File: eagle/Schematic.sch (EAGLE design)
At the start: 28 parts, among them U1 ATMEGA328P, X1 12MHz, X2 16MHz

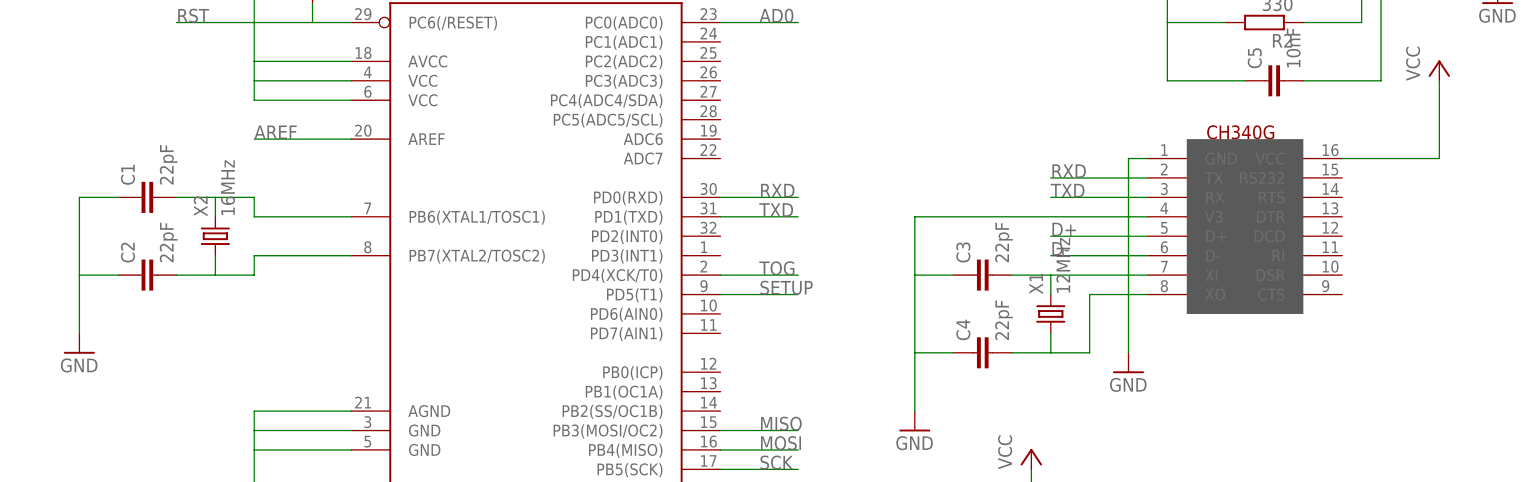
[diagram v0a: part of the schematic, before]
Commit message: Added DTR reset, converted XTAL to smaller ones.
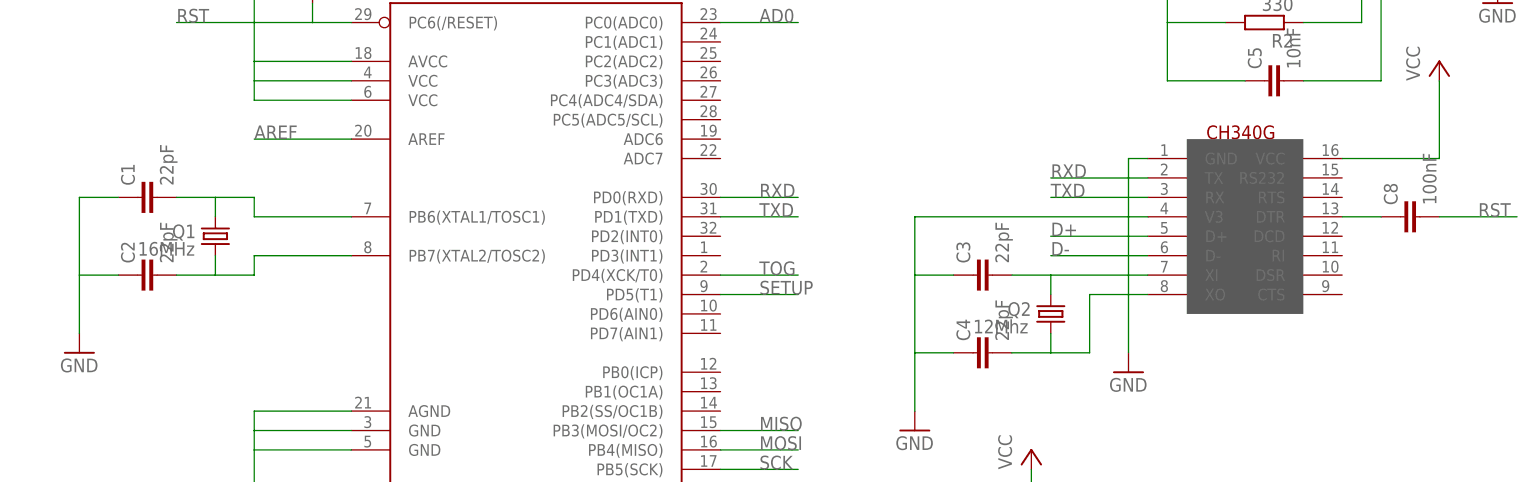
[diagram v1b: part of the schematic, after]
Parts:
- removed X1: 12MHz, IQD-Frequency-Products:CRYSTALS-NOGND-4-HSMX
- removed X2: 16MHz, IQD-Frequency-Products:CRYSTALS-NOGND-4-HSMX
- added C8: 100nF, rcl:C-EUC0603K
- added Q1: 16MHz, seb:MT-OSCILLATOR
- added Q2: 12Mhz, seb:MT-OSCILLATOR
- renumbered U$1 to U2
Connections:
- new net N$6: C8.1, U2.DTR
- net N$2: now also Q2.2; no longer X1.2
- net N$3: now also Q2.1; no longer X1.1
- net N$4: now also Q1.2; no longer X2.2
- net N$5: now also Q1.1; no longer X2.1
- net RST: now also C8.2
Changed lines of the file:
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@@
 <part name="U1" library="SparkFun-DigitalIC" deviceset="ATMEGA328_SMT" device="" value="ATMEGA328P"/>
 <part name="IC1" library="SparkFun-AnalogIC" deviceset="NE555" device="D"/>
-<part name="U$1" library="usb-serial" deviceset="CH340G" device=""/>
+<part name="U2" library="usb-serial" deviceset="CH340G" device=""/>
 <part name="P+1" library="supply1" deviceset="VCC" device=""/>
 <part name="P+2" library="supply1" deviceset="VCC" device=""/>
@@
 <part name="GND2" library="supply1" deviceset="GND" device=""/>
 <part name="GND3" library="supply1" deviceset="GND" device=""/>
-<part name="X1" library="IQD-Frequency-Products" deviceset="CRYSTALS-NOGND" device="-4-HSMX" value="12MHz"/>
-<part name="X2" library="IQD-Frequency-Products" deviceset="CRYSTALS-NOGND" device="-4-HSMX" value="16MHz"/>
 <part name="R1" library="pot" deviceset="TRIM_EU-" device="3223W"/>
 <part name="GND4" library="supply1" deviceset="GND" device=""/>
@@
 <part name="TP7" library="testpad" deviceset="TP" device="TP07R" value="TPTP07R"/>
 <part name="TP8" library="testpad" deviceset="TP" device="TP07R" value="TPTP07R"/>
+<part name="C8" library="rcl" deviceset="C-EU" device="C0603K" value="100nF"/>
+<part name="Q2" library="seb" deviceset="MT-OSCILLATOR" device="" value="12Mhz"/>
+<part name="Q1" library="seb" deviceset="MT-OSCILLATOR" device="" value="16MHz"/>
 </parts>
 <sheets>
@@
 <instance part="U1" gate="G$1" x="68.58" y="43.18"/>
 <instance part="IC1" gate="G$1" x="165.1" y="83.82"/>
-<instance part="U$1" gate="G$1" x="185.42" y="33.02"/>
+<instance part="U2" gate="G$1" x="185.42" y="33.02"/>
 <instance part="P+1" gate="VCC" x="33.02" y="91.44"/>
 <instance part="P+2" gate="VCC" x="187.96" y="63.5"/>
@@
 <instance part="GND2" gate="1" x="33.02" y="5.08"/>
 <instance part="GND3" gate="1" x="195.58" y="71.12"/>
-<instance part="X1" gate="G$1" x="137.16" y="30.48" rot="R90"/>
-<instance part="X2" gate="G$1" x="27.94" y="40.64" rot="R90"/>
 <instance part="R1" gate="1" x="66.04" y="99.06"/>
 <instance part="GND4" gate="1" x="66.04" y="111.76" rot="R180"/>
@@
 <instance part="TP7" gate="G$1" x="71.12" y="0" rot="R90"/>
 <instance part="TP8" gate="G$1" x="71.12" y="2.54" rot="R90"/>
+<instance part="C8" gate="G$1" x="182.88" y="43.18" rot="R90"/>
+<instance part="Q2" gate="G$1" x="137.16" y="30.48" smashed="yes" rot="R90">
+<attribute name="NAME" x="134.62" y="32.004" size="1.778" layer="95" rot="R180"/>
+<attribute name="VALUE" x="127" y="27.94" size="1.778" layer="96"/>
+</instance>
+<instance part="Q1" gate="G$1" x="27.94" y="40.64" smashed="yes" rot="R90">
+<attribute name="NAME" x="25.4" y="42.164" size="1.778" layer="95" rot="R180"/>
+<attribute name="VALUE" x="17.78" y="38.1" size="1.778" layer="96"/>
+</instance>
 </instances>
 <busses>
@@
 <net name="VCC" class="0">
 <segment>
-<pinref part="U$1" gate="G$1" pin="VCC"/>
+<pinref part="U2" gate="G$1" pin="VCC"/>
 <pinref part="P+2" gate="VCC" pin="VCC"/>
 <wire x1="175.26" y1="50.8" x2="187.96" y2="50.8" width="0.1524" layer="91"/>
@@
 </segment>
 <segment>
-<pinref part="U$1" gate="G$1" pin="GND"/>
+<pinref part="U2" gate="G$1" pin="GND"/>
 <wire x1="149.86" y1="50.8" x2="147.32" y2="50.8" width="0.1524" layer="91"/>
 <wire x1="147.32" y1="50.8" x2="147.32" y2="25.4" width="0.1524" layer="91"/>
@@
 <wire x1="119.38" y1="25.4" x2="119.38" y2="17.78" width="0.1524" layer="91"/>
 <pinref part="GND7" gate="1" pin="GND"/>
-<pinref part="U$1" gate="G$1" pin="V3"/>
+<pinref part="U2" gate="G$1" pin="V3"/>
 <wire x1="149.86" y1="43.18" x2="119.38" y2="43.18" width="0.1524" layer="91"/>
 <wire x1="119.38" y1="43.18" x2="119.38" y2="35.56" width="0.1524" layer="91"/>
@@
 </segment>
 <segment>
-<pinref part="U$1" gate="G$1" pin="TX"/>
+<pinref part="U2" gate="G$1" pin="TX"/>
 <wire x1="149.86" y1="48.26" x2="137.16" y2="48.26" width="0.1524" layer="91"/>
 <label x="137.16" y="48.26" size="1.778" layer="95"/>
@@
 <net name="TXD" class="0">
 <segment>
-<pinref part="U$1" gate="G$1" pin="RX"/>
+<pinref part="U2" gate="G$1" pin="RX"/>
 <wire x1="149.86" y1="45.72" x2="137.16" y2="45.72" width="0.1524" layer="91"/>
 <label x="137.16" y="45.72" size="1.778" layer="95"/>
@@
 <net name="N$2" class="0">
 <segment>
-<pinref part="U$1" gate="G$1" pin="XI"/>
+<pinref part="U2" gate="G$1" pin="XI"/>
 <wire x1="149.86" y1="35.56" x2="137.16" y2="35.56" width="0.1524" layer="91"/>
-<pinref part="X1" gate="G$1" pin="2"/>
 <wire x1="137.16" y1="35.56" x2="137.16" y2="33.02" width="0.1524" layer="91"/>
 <pinref part="C3" gate="G$1" pin="2"/>
 <wire x1="137.16" y1="35.56" x2="132.08" y2="35.56" width="0.1524" layer="91"/>
+<pinref part="Q2" gate="G$1" pin="2"/>
 </segment>
 </net>
 <net name="N$3" class="0">
 <segment>
-<pinref part="X1" gate="G$1" pin="1"/>
 <wire x1="137.16" y1="27.94" x2="137.16" y2="25.4" width="0.1524" layer="91"/>
 <wire x1="137.16" y1="25.4" x2="142.24" y2="25.4" width="0.1524" layer="91"/>
 <wire x1="142.24" y1="25.4" x2="142.24" y2="33.02" width="0.1524" layer="91"/>
-<pinref part="U$1" gate="G$1" pin="XO"/>
+<pinref part="U2" gate="G$1" pin="XO"/>
 <wire x1="142.24" y1="33.02" x2="149.86" y2="33.02" width="0.1524" layer="91"/>
 <pinref part="C4" gate="G$1" pin="2"/>
 <wire x1="132.08" y1="25.4" x2="137.16" y2="25.4" width="0.1524" layer="91"/>
+<pinref part="Q2" gate="G$1" pin="1"/>
 </segment>
 </net>
@@
 <wire x1="45.72" y1="43.18" x2="33.02" y2="43.18" width="0.1524" layer="91"/>
 <wire x1="33.02" y1="43.18" x2="33.02" y2="45.72" width="0.1524" layer="91"/>
-<pinref part="X2" gate="G$1" pin="2"/>
 <wire x1="33.02" y1="45.72" x2="27.94" y2="45.72" width="0.1524" layer="91"/>
 <wire x1="27.94" y1="45.72" x2="27.94" y2="43.18" width="0.1524" layer="91"/>
 <pinref part="C1" gate="G$1" pin="2"/>
 <wire x1="22.86" y1="45.72" x2="27.94" y2="45.72" width="0.1524" layer="91"/>
+<pinref part="Q1" gate="G$1" pin="2"/>
 </segment>
 </net>
 <net name="N$5" class="0">
 <segment>
-<pinref part="X2" gate="G$1" pin="1"/>
 <wire x1="27.94" y1="38.1" x2="27.94" y2="35.56" width="0.1524" layer="91"/>
 <wire x1="27.94" y1="35.56" x2="33.02" y2="35.56" width="0.1524" layer="91"/>
@@
 <pinref part="C2" gate="G$1" pin="2"/>
 <wire x1="22.86" y1="35.56" x2="27.94" y2="35.56" width="0.1524" layer="91"/>
+<pinref part="Q1" gate="G$1" pin="1"/>
 </segment>
 </net>
@@
 </segment>
 <segment>
-<pinref part="U$1" gate="G$1" pin="D-"/>
+<pinref part="U2" gate="G$1" pin="D-"/>
 <wire x1="149.86" y1="38.1" x2="137.16" y2="38.1" width="0.1524" layer="91"/>
 <label x="137.16" y="38.1" size="1.778" layer="95"/>
@@
 </segment>
 <segment>
-<pinref part="U$1" gate="G$1" pin="D+"/>
+<pinref part="U2" gate="G$1" pin="D+"/>
 <wire x1="149.86" y1="40.64" x2="137.16" y2="40.64" width="0.1524" layer="91"/>
 <label x="137.16" y="40.64" size="1.778" layer="95"/>
@@
 <label x="76.2" y="-5.08" size="1.778" layer="95"/>
 </segment>
+<segment>
+<pinref part="C8" gate="G$1" pin="2"/>
+<wire x1="187.96" y1="43.18" x2="198.12" y2="43.18" width="0.1524" layer="91"/>
+<label x="193.04" y="43.18" size="1.778" layer="95"/>
+</segment>
 </net>
 <net name="MISO" class="0">
@@
 </segment>
 </net>
+<net name="N$6" class="0">
+<segment>
+<pinref part="U2" gate="G$1" pin="DTR"/>
+<wire x1="175.26" y1="43.18" x2="180.34" y2="43.18" width="0.1524" layer="91"/>
+<pinref part="C8" gate="G$1" pin="1"/>
+</segment>
+</net>

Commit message: Fix PCB errors after first prototype.
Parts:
- added C9: 100nF, rcl:C-EUC0603K
- TP1, TP2, TP3, TP4, TP5, TP6, TP7, TP8: value TPTP07R -> TPTP10R; device testpad:TPTP07R -> testpad:TPTP10R
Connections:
- new net N$7: C9.1, U2.V3
- net GND: now also C9.2; no longer U2.V3
- net MISO: now also U1.PB4(MISO); no longer U1.PB3(MOSI/OC2)
- net MOSI: now also U1.PB3(MOSI/OC2); no longer U1.PB4(MISO)
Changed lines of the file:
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@@
 <?xml version="1.0" encoding="utf-8"?>
 <!DOCTYPE eagle SYSTEM "eagle.dtd">
-<eagle version="7.2.0">
+<eagle version="7.7.0">
 <drawing>
 <settings>
@@
 <grid distance="0.1" unitdist="inch" unit="inch" style="lines" multiple="1" display="no" altdistance="0.01" altunitdist="inch" altunit="inch"/>
 <layers>
-<layer number="1" name="Top" color="4" fill="1" visible="no" active="no"/>
-<layer number="16" name="Bottom" color="1" fill="1" visible="no" active="no"/>
-<layer number="17" name="Pads" color="2" fill="1" visible="no" active="no"/>
-<layer number="18" name="Vias" color="2" fill="1" visible="no" active="no"/>
-<layer number="19" name="Unrouted" color="6" fill="1" visible="no" active="no"/>
-<layer number="20" name="Dimension" color="15" fill="1" visible="no" active="no"/>
-<layer number="21" name="tPlace" color="7" fill="1" visible="no" active="no"/>
-<layer number="22" name="bPlace" color="7" fill="1" visible="no" active="no"/>
-<layer number="23" name="tOrigins" color="15" fill="1" visible="no" active="no"/>
-<layer number="24" name="bOrigins" color="15" fill="1" visible="no" active="no"/>
-<layer number="25" name="tNames" color="7" fill="1" visible="no" active="no"/>
-<layer number="26" name="bNames" color="7" fill="1" visible="no" active="no"/>
-<layer number="27" name="tValues" color="7" fill="1" visible="no" active="no"/>
-<layer number="28" name="bValues" color="7" fill="1" visible="no" active="no"/>
+<layer number="1" name="Top" color="4" fill="1" visible="yes" active="no"/>
+<layer number="16" name="Bottom" color="1" fill="1" visible="yes" active="no"/>
+<layer number="17" name="Pads" color="2" fill="1" visible="yes" active="no"/>
+<layer number="18" name="Vias" color="2" fill="1" visible="yes" active="no"/>
+<layer number="19" name="Unrouted" color="6" fill="1" visible="yes" active="no"/>
+<layer number="20" name="Dimension" color="15" fill="1" visible="yes" active="no"/>
+<layer number="21" name="tPlace" color="7" fill="1" visible="yes" active="no"/>
+<layer number="22" name="bPlace" color="7" fill="1" visible="yes" active="no"/>
+<layer number="23" name="tOrigins" color="15" fill="1" visible="yes" active="no"/>
+<layer number="24" name="bOrigins" color="15" fill="1" visible="yes" active="no"/>
+<layer number="25" name="tNames" color="7" fill="1" visible="yes" active="no"/>
+<layer number="26" name="bNames" color="7" fill="1" visible="yes" active="no"/>
+<layer number="27" name="tValues" color="7" fill="1" visible="yes" active="no"/>
+<layer number="28" name="bValues" color="7" fill="1" visible="yes" active="no"/>
 <layer number="29" name="tStop" color="7" fill="3" visible="no" active="no"/>
 <layer number="30" name="bStop" color="7" fill="6" visible="no" active="no"/>
@@
 <layer number="35" name="tGlue" color="7" fill="4" visible="no" active="no"/>
 <layer number="36" name="bGlue" color="7" fill="5" visible="no" active="no"/>
-<layer number="37" name="tTest" color="7" fill="1" visible="no" active="no"/>
-<layer number="38" name="bTest" color="7" fill="1" visible="no" active="no"/>
+<layer number="37" name="tTest" color="7" fill="1" visible="yes" active="no"/>
+<layer number="38" name="bTest" color="7" fill="1" visible="yes" active="no"/>
 <layer number="39" name="tKeepout" color="4" fill="11" visible="no" active="no"/>
 <layer number="40" name="bKeepout" color="1" fill="11" visible="no" active="no"/>
@@
 <layer number="44" name="Drills" color="7" fill="1" visible="no" active="no"/>
 <layer number="45" name="Holes" color="7" fill="1" visible="no" active="no"/>
-<layer number="46" name="Milling" color="3" fill="1" visible="no" active="no"/>
-<layer number="47" name="Measures" color="7" fill="1" visible="no" active="no"/>
-<layer number="48" name="Document" color="7" fill="1" visible="no" active="no"/>
-<layer number="49" name="Reference" color="7" fill="1" visible="no" active="no"/>
-<layer number="50" name="dxf" color="7" fill="1" visible="no" active="no"/>
-<layer number="51" name="tDocu" color="7" fill="1" visible="no" active="no"/>
-<layer number="52" name="bDocu" color="7" fill="1" visible="no" active="no"/>
-<layer number="53" name="tGND_GNDA" color="7" fill="9" visible="no" active="no"/>
-<layer number="54" name="bGND_GNDA" color="1" fill="9" visible="no" active="no"/>
-<layer number="56" name="wert" color="7" fill="1" visible="no" active="no"/>
-<layer number="57" name="tCAD" color="7" fill="1" visible="no" active="no"/>
+<layer number="46" name="Milling" color="3" fill="1" visible="yes" active="no"/>
+<layer number="47" name="Measures" color="7" fill="1" visible="yes" active="no"/>
+<layer number="48" name="Document" color="7" fill="1" visible="yes" active="no"/>
+<layer number="49" name="Reference" color="7" fill="1" visible="yes" active="no"/>
+<layer number="50" name="dxf" color="7" fill="1" visible="yes" active="no"/>
+<layer number="51" name="tDocu" color="7" fill="1" visible="yes" active="no"/>
+<layer number="52" name="bDocu" color="7" fill="1" visible="yes" active="no"/>
+<layer number="53" name="tGND_GNDA" color="7" fill="9" visible="yes" active="no"/>
+<layer number="54" name="bGND_GNDA" color="1" fill="9" visible="yes" active="no"/>
+<layer number="56" name="wert" color="7" fill="1" visible="yes" active="no"/>
+<layer number="57" name="tCAD" color="7" fill="1" visible="yes" active="no"/>
 <layer number="90" name="Modules" color="5" fill="1" visible="yes" active="yes"/>
 <layer number="91" name="Nets" color="2" fill="1" visible="yes" active="yes"/>
@@
 <part name="D2" library="SparkFun-DiscreteSemi" deviceset="DIODE" device="SOD523"/>
 <part name="GND8" library="supply1" deviceset="GND" device=""/>
-<part name="TP1" library="testpad" deviceset="TP" device="TP07R" value="TPTP07R"/>
-<part name="TP2" library="testpad" deviceset="TP" device="TP07R" value="TPTP07R"/>
-<part name="TP3" library="testpad" deviceset="TP" device="TP07R" value="TPTP07R"/>
-<part name="TP4" library="testpad" deviceset="TP" device="TP07R" value="TPTP07R"/>
-<part name="TP5" library="testpad" deviceset="TP" device="TP07R" value="TPTP07R"/>
+<part name="TP1" library="testpad" deviceset="TP" device="TP10R" value="TPTP10R"/>
+<part name="TP2" library="testpad" deviceset="TP" device="TP10R" value="TPTP10R"/>
+<part name="TP3" library="testpad" deviceset="TP" device="TP10R" value="TPTP10R"/>
+<part name="TP4" library="testpad" deviceset="TP" device="TP10R" value="TPTP10R"/>
+<part name="TP5" library="testpad" deviceset="TP" device="TP10R" value="TPTP10R"/>
 <part name="GND12" library="supply1" deviceset="GND" device=""/>
-<part name="TP6" library="testpad" deviceset="TP" device="TP07R" value="TPTP07R"/>
-<part name="TP7" library="testpad" deviceset="TP" device="TP07R" value="TPTP07R"/>
-<part name="TP8" library="testpad" deviceset="TP" device="TP07R" value="TPTP07R"/>
+<part name="TP6" library="testpad" deviceset="TP" device="TP10R" value="TPTP10R"/>
+<part name="TP7" library="testpad" deviceset="TP" device="TP10R" value="TPTP10R"/>
+<part name="TP8" library="testpad" deviceset="TP" device="TP10R" value="TPTP10R"/>
 <part name="C8" library="rcl" deviceset="C-EU" device="C0603K" value="100nF"/>
 <part name="Q2" library="seb" deviceset="MT-OSCILLATOR" device="" value="12Mhz"/>
 <part name="Q1" library="seb" deviceset="MT-OSCILLATOR" device="" value="16MHz"/>
+<part name="C9" library="rcl" deviceset="C-EU" device="C0603K" value="100nF"/>
 </parts>
 <sheets>
@@
 <attribute name="VALUE" x="17.78" y="38.1" size="1.778" layer="96"/>
 </instance>
+<instance part="C9" gate="G$1" x="129.54" y="43.18" rot="R270"/>
 </instances>
 <busses>
@@
 <wire x1="119.38" y1="25.4" x2="119.38" y2="17.78" width="0.1524" layer="91"/>
 <pinref part="GND7" gate="1" pin="GND"/>
-<pinref part="U2" gate="G$1" pin="V3"/>
-<wire x1="149.86" y1="43.18" x2="119.38" y2="43.18" width="0.1524" layer="91"/>
 <wire x1="119.38" y1="43.18" x2="119.38" y2="35.56" width="0.1524" layer="91"/>
+<pinref part="C9" gate="G$1" pin="2"/>
+<wire x1="119.38" y1="43.18" x2="124.46" y2="43.18" width="0.1524" layer="91"/>
 </segment>
 <segment>
@@
 <net name="MISO" class="0">
 <segment>
+<pinref part="TP4" gate="G$1" pin="TP"/>
+<wire x1="73.66" y1="-7.62" x2="81.28" y2="-7.62" width="0.1524" layer="91"/>
+<label x="76.2" y="-7.62" size="1.778" layer="95"/>
+</segment>
+<segment>
+<pinref part="U1" gate="G$1" pin="PB4(MISO)"/>
+<wire x1="93.98" y1="12.7" x2="104.14" y2="12.7" width="0.1524" layer="91"/>
+<label x="99.06" y="12.7" size="1.778" layer="95"/>
+</segment>
+</net>
+<net name="MOSI" class="0">
+<segment>
+<pinref part="TP3" gate="G$1" pin="TP"/>
+<wire x1="73.66" y1="-10.16" x2="81.28" y2="-10.16" width="0.1524" layer="91"/>
+<label x="76.2" y="-10.16" size="1.778" layer="95"/>
+</segment>
+<segment>
 <pinref part="U1" gate="G$1" pin="PB3(MOSI/OC2)"/>
 <wire x1="93.98" y1="15.24" x2="104.14" y2="15.24" width="0.1524" layer="91"/>
 <label x="99.06" y="15.24" size="1.778" layer="95"/>
-</segment>
-<segment>
-<pinref part="TP4" gate="G$1" pin="TP"/>
-<wire x1="73.66" y1="-7.62" x2="81.28" y2="-7.62" width="0.1524" layer="91"/>
-<label x="76.2" y="-7.62" size="1.778" layer="95"/>
-</segment>
-</net>
-<net name="MOSI" class="0">
-<segment>
-<pinref part="U1" gate="G$1" pin="PB4(MISO)"/>
-<wire x1="93.98" y1="12.7" x2="104.14" y2="12.7" width="0.1524" layer="91"/>
-<label x="99.06" y="12.7" size="1.778" layer="95"/>
-</segment>
-<segment>
-<pinref part="TP3" gate="G$1" pin="TP"/>
-<wire x1="73.66" y1="-10.16" x2="81.28" y2="-10.16" width="0.1524" layer="91"/>
-<label x="76.2" y="-10.16" size="1.778" layer="95"/>
 </segment>
 </net>
@@
 </segment>
 </net>
+<net name="N$7" class="0">
+<segment>
+<pinref part="C9" gate="G$1" pin="1"/>
+<pinref part="U2" gate="G$1" pin="V3"/>
+<wire x1="132.08" y1="43.18" x2="149.86" y2="43.18" width="0.1524" layer="91"/>
+</segment>
+</net>
